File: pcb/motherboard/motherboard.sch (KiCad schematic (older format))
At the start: 16 parts, among them J1 749801122R, J2 DISPLAY, J3 BARREL_JACK, J4 Micro_SD, J5 VBAT, J6 DEBUG, U1 ARIA-G25, U2 CAT811

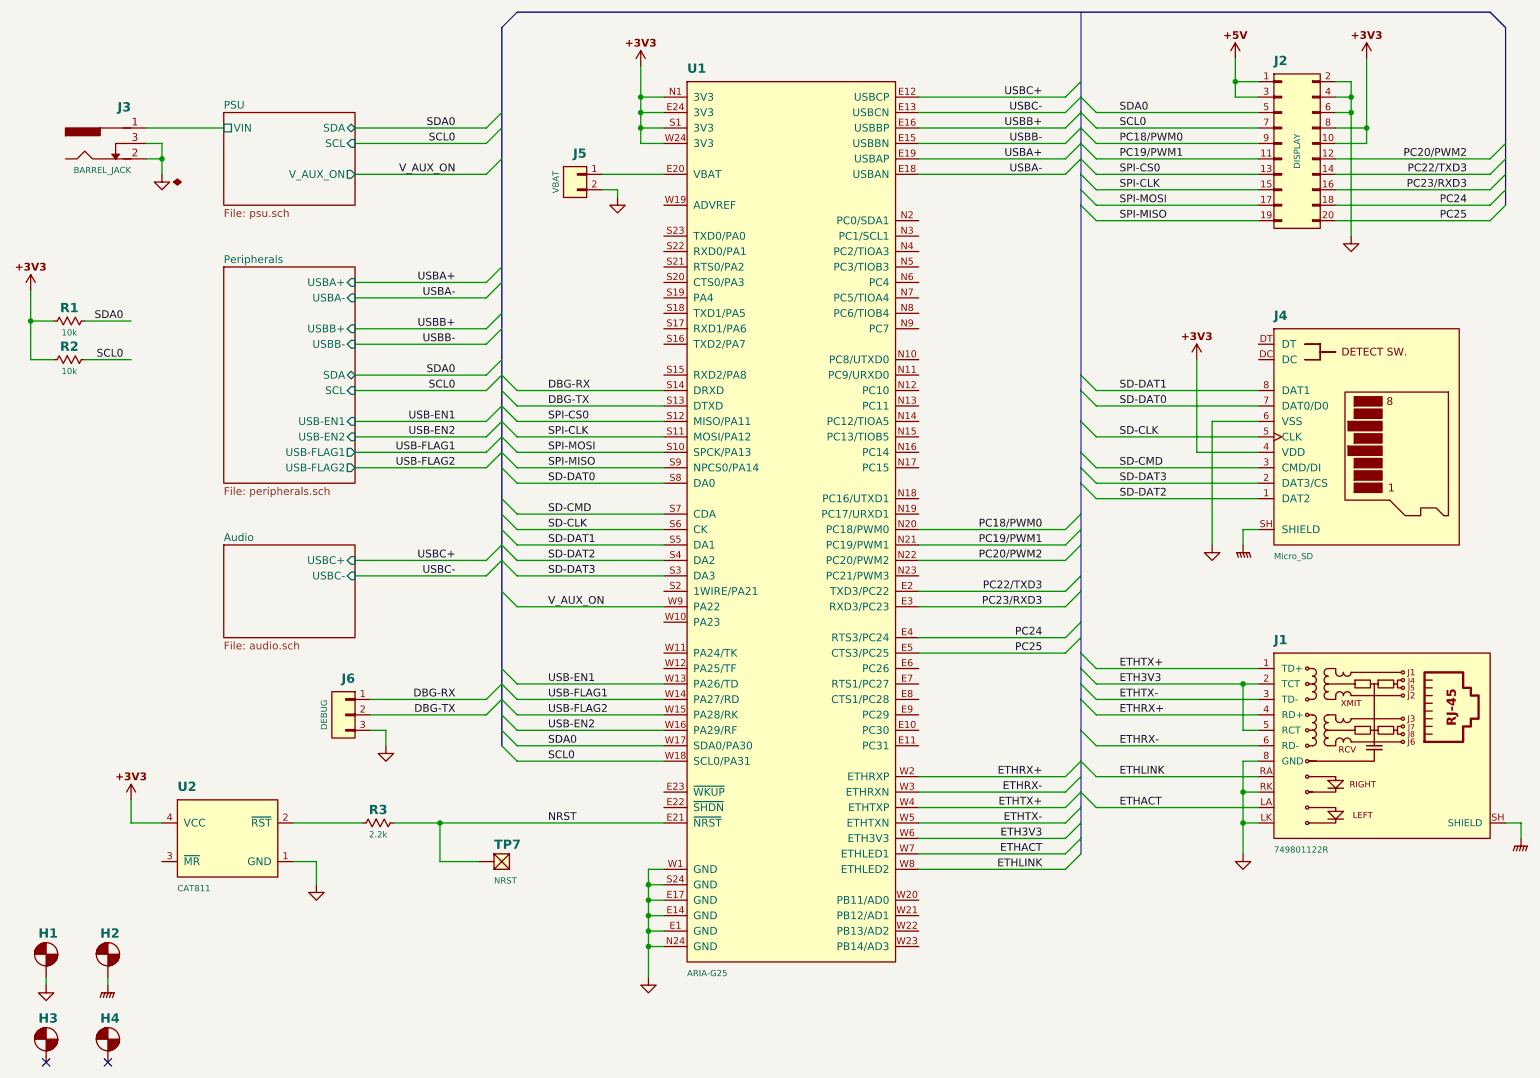
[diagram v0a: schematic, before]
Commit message: Changed crystal location for PCM2704
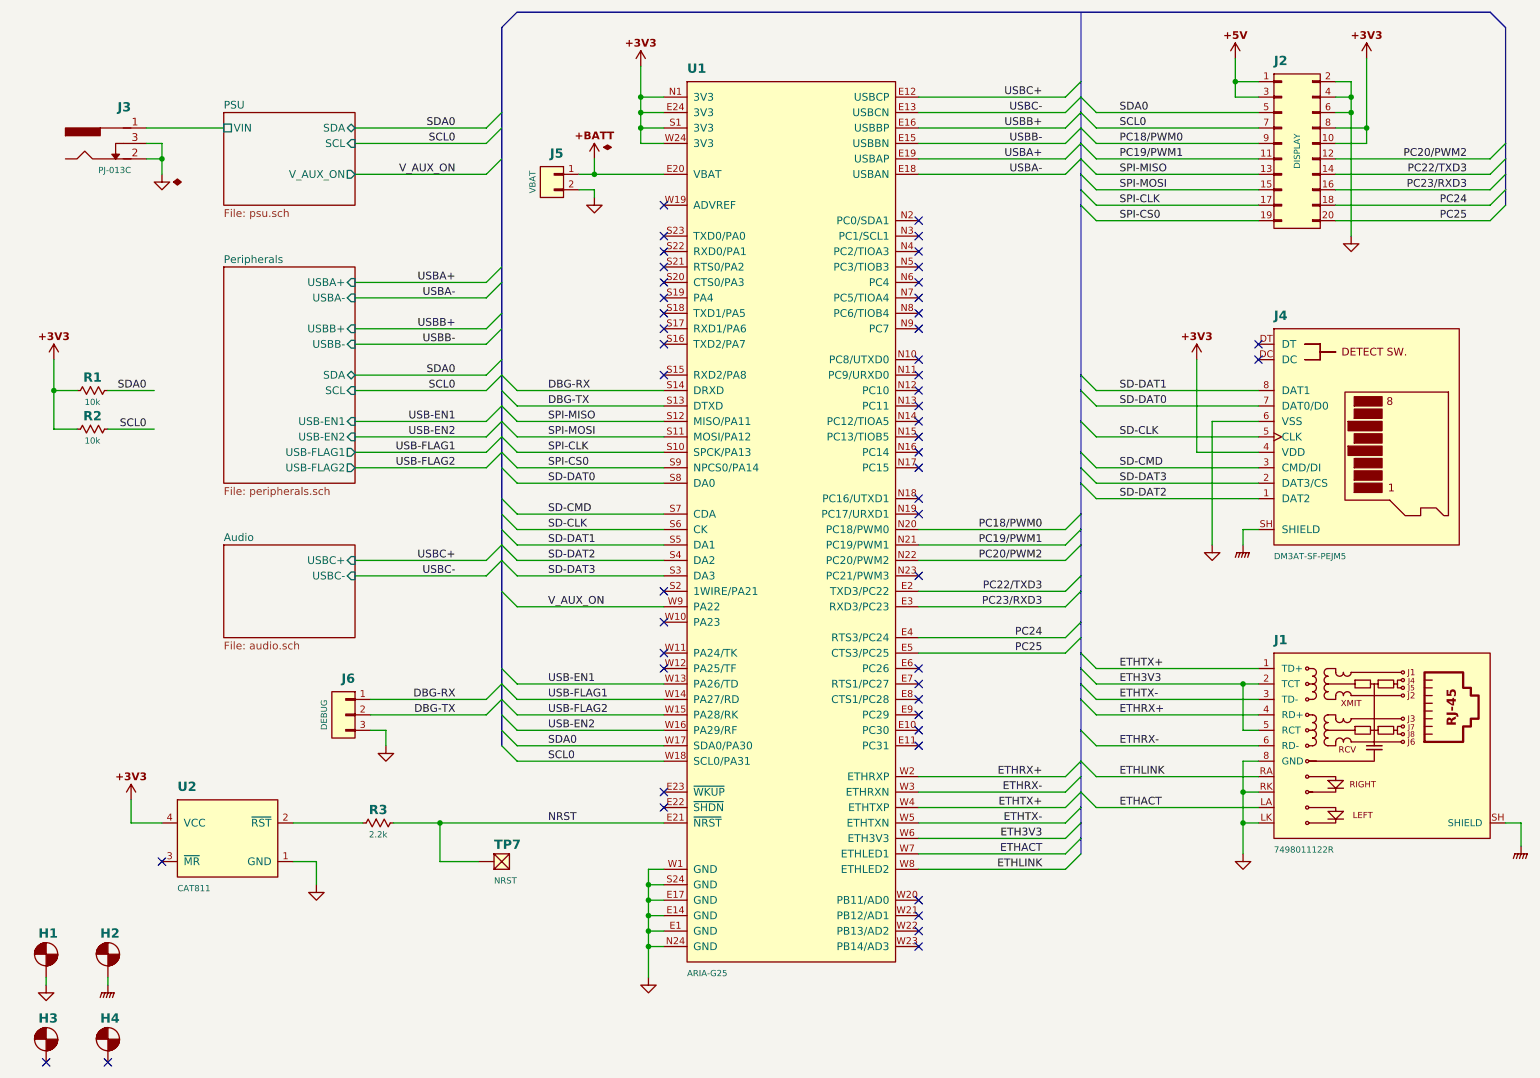
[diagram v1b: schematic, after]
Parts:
- H1, H2, H3, H4: footprint Misc:Hole-Screw-#4 -> Conn-Wire-Pads:Hole-Screw-#4
- J1: value 749801122R -> 7498011122R
- J3: value BARREL_JACK -> PJ-013C; footprint Conn-IO:CUI-PJ-013C -> Conn-Power:CUI-PJ-031CH
- J4: value Micro_SD -> DM3AT-SF-PEJM5
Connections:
- net SPI-CLK: now also J2.17 (P17), U1.S10 (SPCK/PA13); no longer J2.15 (P15), U1.S11 (MOSI/PA12)
- net SPI-CS0: now also J2.19 (P19), U1.S9 (NPCS0/PA14); no longer J2.13 (P13), U1.S12 (MISO/PA11)
- net SPI-MISO: now also J2.13 (P13), U1.S12 (MISO/PA11); no longer J2.19 (P19), U1.S9 (NPCS0/PA14)
- net SPI-MOSI: now also J2.15 (P15), U1.S11 (MOSI/PA12); no longer J2.17 (P17), U1.S10 (SPCK/PA13)
- net +BATT: now reaches J5.1 (P1), U1.E20 (VBAT)
- no-connect marks 2 -> 50
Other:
- moved on the sheet: J5, R1, R2

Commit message: Tidy up motherboard schematic
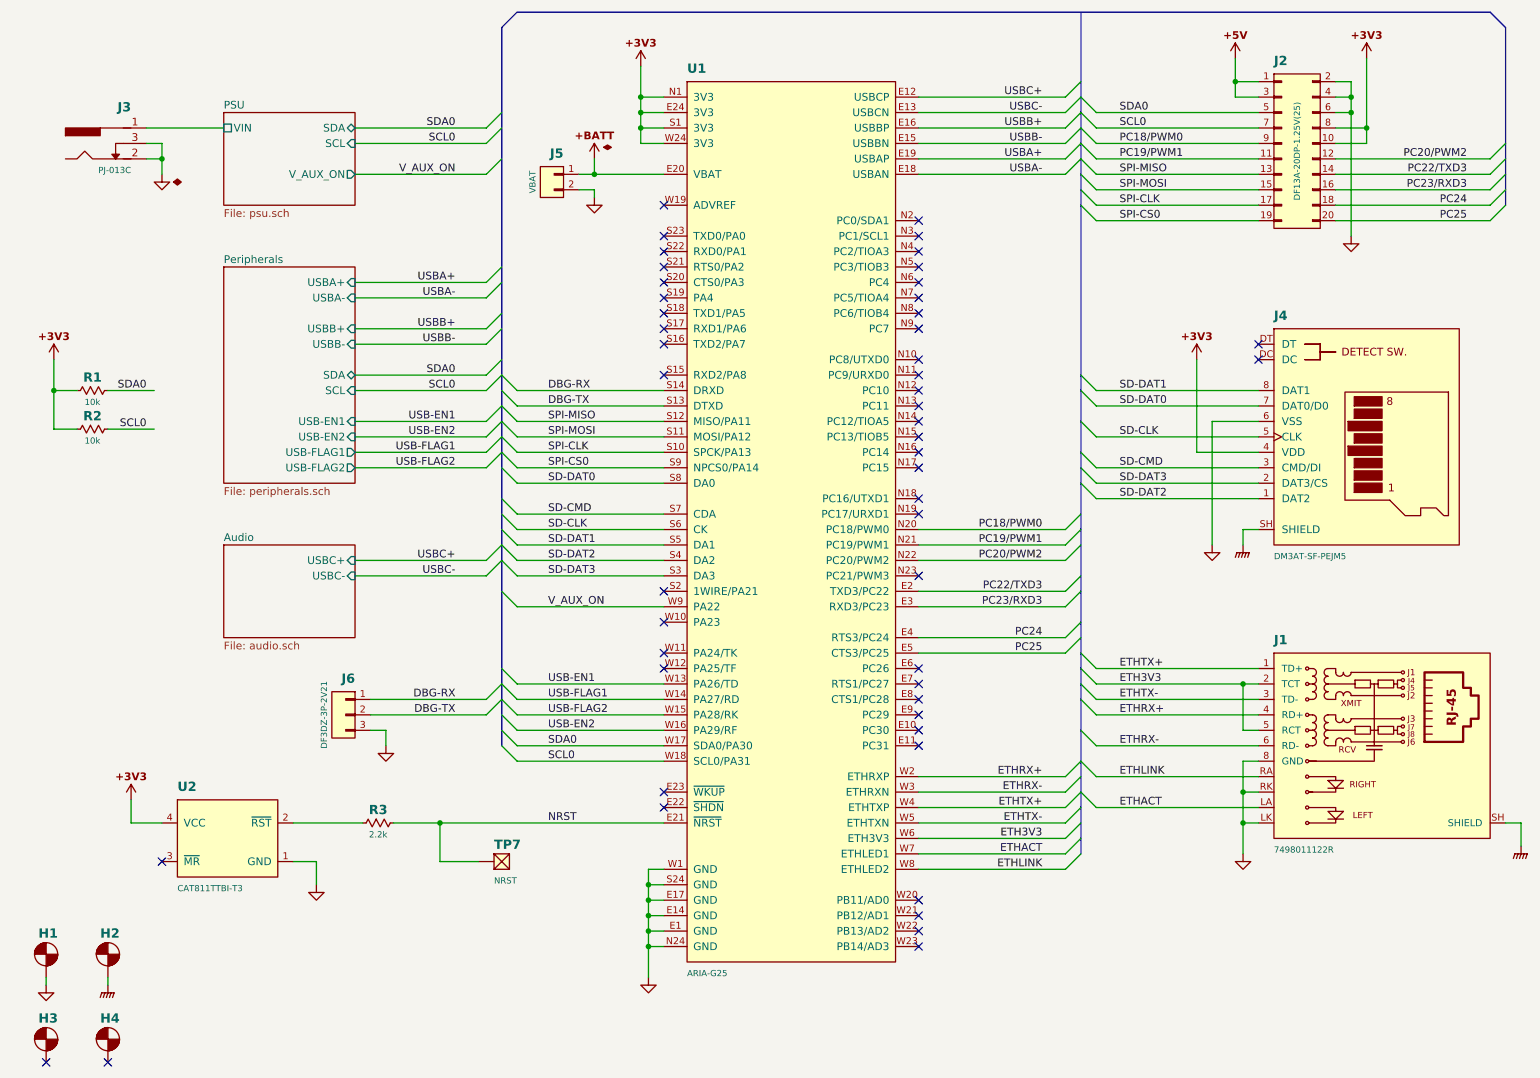
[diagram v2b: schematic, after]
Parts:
- H1, H2, H3, H4, J5, TP7: Family (none) -> Virtual
- J1: Family (none) -> Connector; MFG (none) -> Wurth
- J2: value DISPLAY -> DF13A-20DP-1.25V(25); Family (none) -> Connector; MFG (none) -> Hirose
- J3: Family (none) -> Connector; MFG (none) -> CUI Inc
- J4: Family (none) -> Connector; MFG (none) -> Hirose
- J6: value DEBUG -> DF3DZ-3P-2V21; Family (none) -> Connector; MFG (none) -> Hirose
- R1, R2, R3: Family (none) -> Passive
- U1: Family (none) -> IC; MFG (none) -> ACME Systems
- U2: value CAT811 -> CAT811TTBI-T3; Family (none) -> IC
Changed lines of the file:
@@
 Sheet 1 4
 Title "MOTHERBOARD"
-Date "Wed 18 Mar 2015"
+Date "Sun 12 Apr 2015"
 Rev "A"
 Comp ""
@@
 F 2 "Misc:ARIA-G25" H 4950 1200 40  0001 L CNN
 F 3 "" H 3000 5850 60  0001 C CNN
+F 4 "IC" H 5600 4200 60  0001 C CNN "Family"
+F 5 "ACME Systems" H 5600 4200 60  0001 C CNN "MFG"
 	1    5600 4200
 	1    0    0    -1
@@
 F 2 "Conn-IO:RJ45-WURTH-7498011122R" H 8750 4900 40  0001 L CNN
 F 3 "" V 10075 5875 60  0000 C CNN
+F 4 "Connector" H 9450 5650 60  0001 C CNN "Family"
+F 5 "Wurth" H 9450 5650 60  0001 C CNN "MFG"
 	1    9450 5650
 	1    0    0    -1
@@
 P 8900 1800
 F 0 "J2" H 8750 2350 60  0000 L BNB
-F 1 "DISPLAY" V 8900 1800 40  0000 C CNN
+F 1 "DF13A-20DP-1.25V(25)" V 8900 1800 40  0000 C CNN
 F 2 "Conn-Hirose:DF13A-20DP-1.25" H 8900 600 60  0001 C CNN
 F 3 "" H 8900 600 60  0001 C CNN
+F 4 "Connector" H 8900 1800 60  0001 C CNN "Family"
+F 5 "Hirose" H 8900 1800 60  0001 C CNN "MFG"
 	1    8900 1800
 	1    0    0    -1
@@
 F 2 "Conn-Power:CUI-PJ-031CH" H 1300 1750 60  0001 C CNN
 F 3 "" H 1300 1750 60  0001 C CNN
+F 4 "Connector" H 1250 1750 60  0001 C CNN "Family"
+F 5 "CUI Inc" H 1250 1750 60  0001 C CNN "MFG"
 	1    1250 1750
 	-1   0    0    -1
-$EndComp
-$Comp
-L Micro_SD J4
-U 1 1 54FB8E06
-P 9350 3700
-F 0 "J4" H 8750 4500 60  0000 L BNB
-F 1 "DM3AT-SF-PEJM5" H 8750 3000 40  0000 L TNN
-F 2 "Conn-IO:HIROSE-MICROSD-DM3AT-SF" H 8750 2800 40  0001 L CNN
-F 3 "" V 9310 3640 60  0001 C CNN
-	1    9350 3700
-	1    0    0    -1
 $EndComp
 Entry Wire Line
@@
 P 2750 5450
 F 0 "J6" H 2700 5650 60  0000 L BNB
-F 1 "DEBUG" V 2900 5450 40  0000 C CNN
+F 1 "DF3DZ-3P-2V21" V 2900 5450 40  0000 C CNN
 F 2 "Conn-Hirose:DF3DZ-3P-2VXX" H 2750 5450 60  0001 C CNN
 F 3 "" H 2750 5450 60  0001 C CNN
+F 4 "Connector" H 2750 5450 60  0001 C CNN "Family"
+F 5 "Hirose" H 2750 5450 60  0001 C CNN "MFG"
 	1    2750 5450
 	-1   0    0    -1
@@
 F 2 "Conn-Wire-Pads:WP-75mil-1x02" H 4100 2000 60  0001 C CNN
 F 3 "" H 4100 2000 60  0001 C CNN
+F 4 "Virtual" H 4100 2000 60  0001 C CNN "Family"
 	1    4100 2000
 	-1   0    0    -1
@@
 F 3 "" H 1100 3450 60  0000 C CNN
 F 4 "-" H 1100 3510 45  0001 C CNN "Part"
+F 5 "Passive" H 1100 3350 60  0001 C CNN "Family"
 	1    1100 3350
 	1    0    0    -1
@@
 F 3 "" H 1100 3700 60  0000 C CNN
 F 4 "-" H 1100 3760 45  0001 C CNN "Part"
+F 5 "Passive" H 1100 3600 60  0001 C CNN "Family"
 	1    1100 3600
 	1    0    0    -1
@@
 P 2000 6250
 F 0 "U2" H 1650 6550 60  0000 L BNB
-F 1 "CAT811" H 1650 5950 40  0000 L TNN
+F 1 "CAT811TTBI-T3" H 1650 5950 40  0000 L TNN
 F 2 "SMT-SOT:SOT-143" H 1650 5875 40  0001 L TNN
 F 3 "" H 1650 6550 50  0000 C CNN
+F 4 "IC" H 2000 6250 60  0001 C CNN "Family"
 	1    2000 6250
 	1    0    0    -1
@@
 F 3 "" H 2950 6250 60  0000 C CNN
 F 4 "-" H 2950 6310 45  0001 C CNN "Part"
+F 5 "Passive" H 2950 6150 60  0001 C CNN "Family"
 	1    2950 6150
 	1    0    0    -1
@@
 	7600 5150 8650 5150
 Wire Wire Line
-	7600 5250 8550 5250
-Wire Wire Line
-	8550 5250 8650 5250
+	7600 5250 8650 5250
 Wire Wire Line
 	7600 5350 8650 5350
@@
 	8550 6150 8650 6150
 Wire Wire Line
-	8550 5750 8550 5950
-Wire Wire Line
-	8550 5950 8550 6150
-Wire Wire Line
-	8550 6150 8550 6350
+	8550 5750 8550 6350
 Wire Wire Line
 	8650 5950 8550 5950
@@
 Connection ~ 8550 5950
 Wire Bus Line
-	7500 900  7500 1350
-Wire Bus Line
-	7500 1350 7500 1450
-Wire Bus Line
-	7500 1450 7500 1550
-Wire Bus Line
-	7500 1550 7500 1650
-Wire Bus Line
-	7500 1650 7500 1750
-Wire Bus Line
-	7500 1750 7500 1850
-Wire Bus Line
-	7500 1850 7500 1950
-Wire Bus Line
-	7500 1950 7500 2050
-Wire Bus Line
-	7500 2050 7500 2150
-Wire Bus Line
-	7500 2150 7500 3250
-Wire Bus Line
-	7500 3250 7500 3350
-Wire Bus Line
-	7500 3350 7500 3550
-Wire Bus Line
-	7500 3550 7500 3750
-Wire Bus Line
-	7500 3750 7500 3850
-Wire Bus Line
-	7500 3850 7500 3950
-Wire Bus Line
-	7500 3950 7500 4150
-Wire Bus Line
-	7500 4150 7500 4250
-Wire Bus Line
-	7500 4250 7500 4350
-Wire Bus Line
-	7500 4350 7500 4550
-Wire Bus Line
-	7500 4550 7500 4650
-Wire Bus Line
-	7500 4650 7500 4850
-Wire Bus Line
-	7500 4850 7500 4950
-Wire Bus Line
-	7500 4950 7500 5050
-Wire Bus Line
-	7500 5050 7500 5150
-Wire Bus Line
-	7500 5150 7500 5250
-Wire Bus Line
-	7500 5250 7500 5350
-Wire Bus Line
-	7500 5350 7500 5550
-Wire Bus Line
-	7500 5550 7500 5750
-Wire Bus Line
-	7500 5750 7500 5850
-Wire Bus Line
-	7500 5850 7500 5950
-Wire Bus Line
-	7500 5950 7500 6050
-Wire Bus Line
-	7500 6050 7500 6150
-Wire Bus Line
-	7500 6150 7500 6250
-Wire Bus Line
-	7500 6250 7500 6350
+	7500 900  7500 6350
 Wire Wire Line
 	7400 1450 6450 1450
@@
 	10150 900  10250 1000
 Wire Bus Line
-	10250 1000 10250 1750
-Wire Bus Line
-	10250 1750 10250 1850
-Wire Bus Line
-	10250 1850 10250 1950
-Wire Bus Line
-	10250 1950 10250 2050
-Wire Bus Line
-	10250 2050 10250 2150
+	10250 1000 10250 2150
 Wire Bus Line
 	3850 900  3750 1000
 Wire Bus Line
-	3750 1000 3750 1550
-Wire Bus Line
-	3750 1550 3750 1650
-Wire Bus Line
-	3750 1650 3750 1850
-Wire Bus Line
-	3750 1850 3750 2550
-Wire Bus Line
-	3750 2550 3750 2650
-Wire Bus Line
-	3750 2650 3750 2850
-Wire Bus Line
-	3750 2850 3750 2950
-Wire Bus Line
-	3750 2950 3750 3150
-Wire Bus Line
-	3750 3150 3750 3250
-Wire Bus Line
-	3750 3250 3750 3350
-Wire Bus Line
-	3750 3350 3750 3450
-Wire Bus Line
-	3750 3450 3750 3550
-Wire Bus Line
-	3750 3550 3750 3650
-Wire Bus Line
-	3750 3650 3750 3750
-Wire Bus Line
-	3750 3750 3750 3850
-Wire Bus Line
-	3750 3850 3750 4050
-Wire Bus Line
-	3750 4050 3750 4150
-Wire Bus Line
-	3750 4150 3750 4250
-Wire Bus Line
-	3750 4250 3750 4350
-Wire Bus Line
-	3750 4350 3750 4450
-Wire Bus Line
-	3750 4450 3750 4650
-Wire Bus Line
-	3750 4650 3750 5150
-Wire Bus Line
-	3750 5150 3750 5250
-Wire Bus Line
-	3750 5250 3750 5350
-Wire Bus Line
-	3750 5350 3750 5450
-Wire Bus Line
-	3750 5450 3750 5550
-Wire Bus Line
-	3750 5550 3750 5650
+	3750 1000 3750 5650
 Wire Wire Line
 	4800 5750 3850 5750
@@
 	1450 1850 1550 1850
 Wire Wire Line
-	1550 1750 1550 1850
-Wire Wire Line
-	1550 1850 1550 1950
+	1550 1750 1550 1950
 Wire Wire Line
 	1450 1750 1550 1750
@@
 	3850 3350 4800 3350
 Wire Wire Line
-	4800 1950 4350 1950
-Wire Wire Line
-	4350 1950 4250 1950
+	4250 1950 4800 1950
 Wire Wire Line
 	4350 2050 4250 2050
@@
 	4800 4750 3850 4750
 Wire Wire Line
-	850  3150 850  3350
-Wire Wire Line
-	850  3350 850  3600
+	850  3150 850  3600
 Wire Wire Line
 	850  3350 1000 3350
@@
 	2400 6150 2850 6150
 Wire Wire Line
-	3050 6150 3350 6150
-Wire Wire Line
-	3350 6150 4800 6150
+	3050 6150 4800 6150
 Wire Wire Line
 	4350 2050 4350 2100
@@
 	4800 6450 4700 6450
 Wire Wire Line
-	4700 6450 4700 6550
-Wire Wire Line
-	4700 6550 4700 6650
-Wire Wire Line
-	4700 6650 4700 6750
-Wire Wire Line
-	4700 6750 4700 6850
-Wire Wire Line
-	4700 6850 4700 6950
-Wire Wire Line
-	4700 6950 4700 7150
+	4700 6450 4700 7150
 Wire Wire Line
 	4800 6950 4700 6950
@@
 $EndComp
 Wire Wire Line
-	4650 1250 4650 1450
-Wire Wire Line
-	4650 1450 4650 1550
-Wire Wire Line
-	4650 1550 4650 1650
-Wire Wire Line
-	4650 1650 4650 1750
+	4650 1250 4650 1750
 Wire Wire Line
 	4650 1450 4800 1450
@@
 F 2 "Conn-Wire-Pads:Hole-Screw-#4" H 1250 6825 40  0001 L TNN
 F 3 "" H 1150 7075 60  0001 C CNN
+F 4 "Virtual" H 1200 7000 60  0001 C CNN "Family"
 	1    1200 7000
 	1    0    0    -1
@@
 F 2 "Conn-Wire-Pads:Hole-Screw-#4" H 850 7375 40  0001 L TNN
 F 3 "" H 750 7625 60  0001 C CNN
+F 4 "Virtual" H 800 7550 60  0001 C CNN "Family"
 	1    800  7550
 	1    0    0    -1
@@
 F 2 "Conn-Wire-Pads:Hole-Screw-#4" H 850 6825 40  0001 L TNN
 F 3 "" H 750 7075 60  0001 C CNN
+F 4 "Virtual" H 800 7000 60  0001 C CNN "Family"
 	1    800  7000
 	1    0    0    -1
@@
 F 2 "Conn-Wire-Pads:Hole-Screw-#4" H 1250 7375 40  0001 L TNN
 F 3 "" H 1150 7625 60  0001 C CNN
+F 4 "Virtual" H 1200 7550 60  0001 C CNN "Family"
 	1    1200 7550
 	1    0    0    -1
@@
 $EndComp
 Wire Wire Line
-	8500 1200 8500 1350
-Wire Wire Line
-	8500 1350 8500 1450
+	8500 1200 8500 1450
 Wire Wire Line
 	8500 1350 8650 1350
@@
 	9150 1350 9250 1350
 Wire Wire Line
-	9250 1350 9250 1450
-Wire Wire Line
-	9250 1450 9250 1550
-Wire Wire Line
-	9250 1550 9250 2350
+	9250 1350 9250 2350
 Wire Wire Line
 	9150 1450 9250 1450
@@
 $EndComp
 Wire Wire Line
-	9350 1200 9350 1650
-Wire Wire Line
-	9350 1650 9350 1750
+	9350 1200 9350 1750
 Wire Wire Line
 	9350 1650 9150 1650
@@
 F 2 "Conn-Wire-Pads:TEST-POINT-50" H 3600 6375 60  0001 C CNN
 F 3 "" H 3700 6475 60  0001 C CNN
+F 4 "Virtual" H 3750 6400 60  0001 C CNN "Family"
 	1    3750 6400
 	1    0    0    -1
@@
 	1    0    0    -1
 $EndComp
+$Comp
+L Micro_SD J4
+U 1 1 54FB8E06
+P 9350 3700
+F 0 "J4" H 8750 4500 60  0000 L BNB
+F 1 "DM3AT-SF-PEJM5" H 8750 3000 40  0000 L TNN
+F 2 "Conn-IO:HIROSE-MICROSD-DM3AT-SF" H 8750 2800 40  0001 L CNN
+F 3 "" V 9310 3640 60  0001 C CNN
+F 4 "Connector" H 9350 3700 60  0001 C CNN "Family"
+F 5 "Hirose" H 9350 3700 60  0001 C CNN "MFG"
+	1    9350 3700
+	1    0    0    -1
+$EndComp
